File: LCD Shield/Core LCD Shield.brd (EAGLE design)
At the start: 115.6 x 54.6 mm, 7 parts

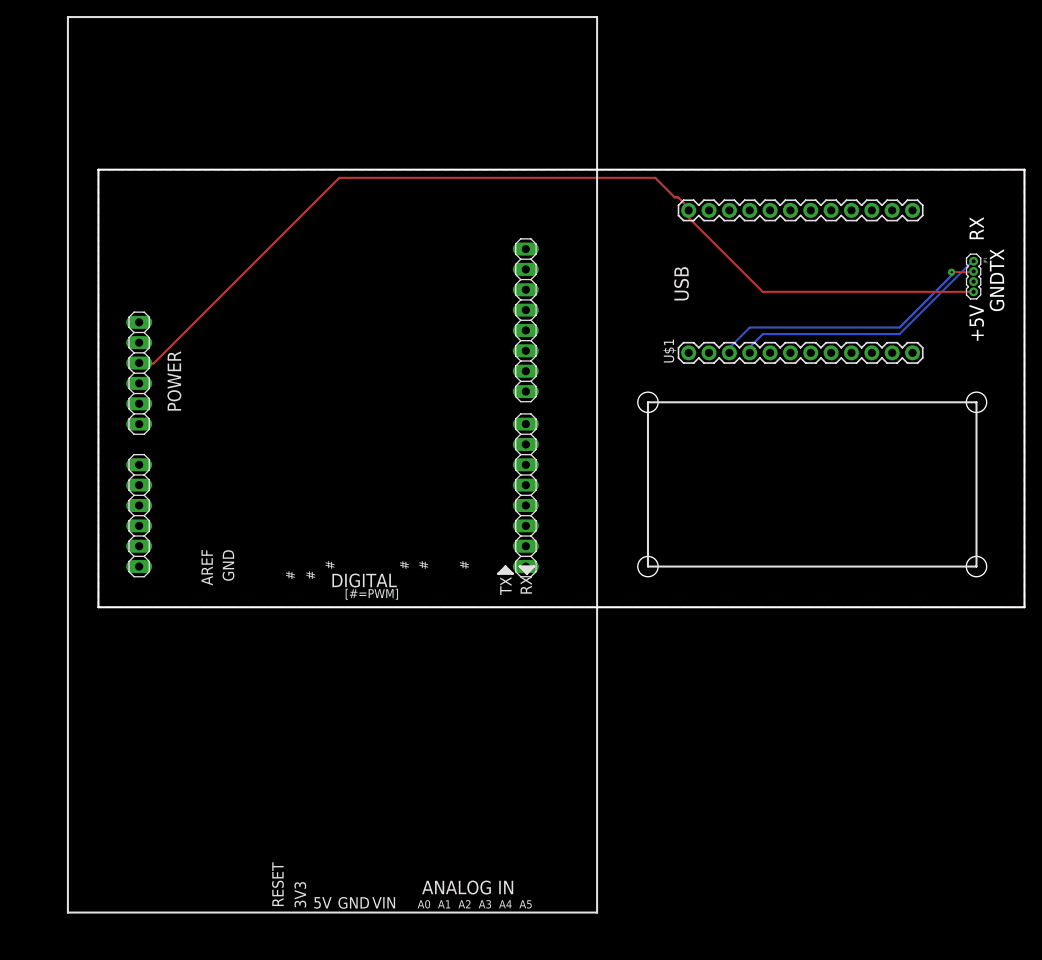
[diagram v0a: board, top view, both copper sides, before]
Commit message: WIP: Created infinity camera from Shield Shield template.
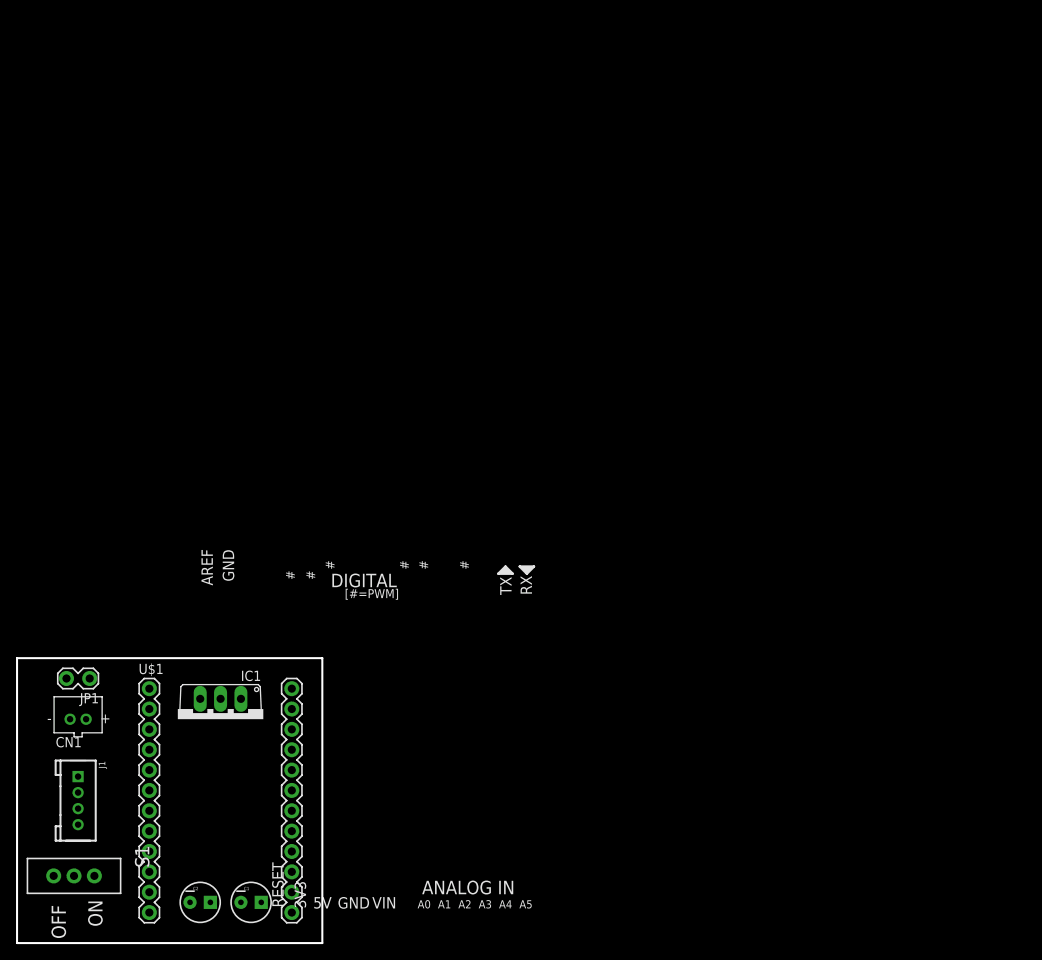
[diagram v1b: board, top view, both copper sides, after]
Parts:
- removed AD, POWER: (no value), pinhead:1X06
- removed IOH, IOL: (no value), pinhead:1X08
- removed U$2: (no value), Spark:SPARK_LOGO
- added C1: 10uF, SparkFun-Capacitors:CPOL-RADIAL-10UF-25V
- added C2: 1uF, SparkFun-Capacitors:CPOL-RADIAL-10UF-25V
- added CN1: (no value), adafruit:JST-PH-2-THM
- added IC1: MC33269T-5.0, linear:TO220V
- added J1: TWIG_2.0-DIP-FEMALE, Connector:2.0_1X4
- added S1: (no value), SparkFun-Electromechanical:SWITCH-SPDT
- JP1: device SparkFun-Connectors:1X04-1.27MM -> SparkFun-Connectors:1X02_LOCK
- moved JP1 122.1 mm to (8.89, 33.0), turned to 180 degrees
- moved U$1 97.1 mm to (25.4, 17.8), turned to 0 degrees
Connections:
- removed net RAW: U$1.1
- new net +3V3: U$1.24
- new net N1: C1.1, IC1.2, S1.2
- new net RESET: U$1.23
- new net VIN: C2.1, CN1.1, IC1.3, JP1.1, U$1.1
- net +5V: now also J1.3, S1.1; no longer JP1.4, POWER.3, U$1.24
- net GND: now also C1.2, C2.2, CN1.2, IC1.1, J1.4, JP1.2; no longer IOH.7, JP1.3, POWER.4, POWER.5
- net RX: now also J1.2; no longer JP1.1
- net TX: now also J1.1; no longer JP1.2
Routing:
- net +5V: track 120.9 -> 0.00 mm
- net TX: track 35.5 -> 0.00 mm, vias 1 -> 0
- net RX: track 33.1 -> 0.00 mm
- removed copper zone on layer 1, net GND
- removed copper zone on layer 16, net GND
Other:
- board size 115.6 x 54.6 mm -> 38.1 x 35.6 mm
- board text added: "OFF"
- board text added: "ON"
- board text removed: "+5V"
- board text removed: "USB"
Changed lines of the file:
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@@
 <rectangle x1="90.7098" y1="32.6327" x2="94.5833" y2="32.6454" layer="201"/>
 <rectangle x1="87.5348" y1="32.6327" x2="90.7098" y2="32.6454" layer="201"/>
-<wire x1="6.35" y1="3.81" x2="6.35" y2="115.57" width="0.254" layer="21"/>
-<wire x1="6.35" y1="115.57" x2="72.39" y2="115.57" width="0.254" layer="21"/>
-<wire x1="72.39" y1="115.57" x2="72.39" y2="3.81" width="0.254" layer="21"/>
-<wire x1="72.39" y1="3.81" x2="6.35" y2="3.81" width="0.254" layer="21"/>
-<hole x="119.74" y="46.99" drill="2.54"/>
-<hole x="78.74" y="46.99" drill="2.54"/>
-<hole x="78.74" y="67.49" drill="2.54"/>
-<hole x="119.74" y="67.49" drill="2.54"/>
-<wire x1="10.16" y1="41.91" x2="10.16" y2="96.52" width="0.254" layer="20"/>
-<wire x1="10.16" y1="96.52" x2="125.73" y2="96.52" width="0.254" layer="20"/>
-<wire x1="125.73" y1="96.52" x2="125.73" y2="41.91" width="0.254" layer="20"/>
-<wire x1="125.73" y1="41.91" x2="10.16" y2="41.91" width="0.254" layer="20"/>
-<text x="120.65" y="74.93" size="1.778" layer="20" font="vector" ratio="15" rot="R90">+5V</text>
-<text x="123.19" y="78.74" size="1.778" layer="20" font="vector" ratio="15" rot="R90">GND</text>
-<text x="123.19" y="83.82" size="1.778" layer="20" font="vector" ratio="15" rot="R90">TX</text>
-<text x="120.65" y="87.63" size="1.778" layer="20" font="vector" ratio="15" rot="R90">RX</text>
-<wire x1="78.74" y1="46.99" x2="78.74" y2="67.49" width="0.254" layer="21"/>
-<wire x1="78.74" y1="67.49" x2="119.74" y2="67.49" width="0.254" layer="21"/>
-<wire x1="119.74" y1="67.49" x2="119.74" y2="46.99" width="0.254" layer="21"/>
-<wire x1="119.74" y1="46.99" x2="78.74" y2="46.99" width="0.254" layer="21"/>
-<text x="83.82" y="80.01" size="1.778" layer="21" font="vector" ratio="15" rot="R90">USB</text>
+<text x="10.668" y="2.032" size="1.778" layer="21" ratio="15" rot="R90">ON</text>
+<text x="6.096" y="0.508" size="1.778" layer="21" ratio="15" rot="R90">OFF</text>
+<wire x1="0" y1="0" x2="0" y2="35.56" width="0.254" layer="20"/>
+<wire x1="0" y1="35.56" x2="38.1" y2="35.56" width="0.254" layer="20"/>
+<wire x1="38.1" y1="35.56" x2="38.1" y2="0" width="0.254" layer="20"/>
+<wire x1="38.1" y1="0" x2="0" y2="0" width="0.254" layer="20"/>
 </plain>
 <attributes>
@@
 </autorouter>
 <elements>
-<element name="IOL" library="pinhead" package="1X08" value="" x="63.5" y="55.88" smashed="yes" rot="R90">
-<attribute name="VALUE" x="66.675" y="45.72" size="1.27" layer="27" rot="R90"/>
-</element>
-<element name="IOH" library="pinhead" package="1X08" value="" x="63.5" y="77.724" smashed="yes" rot="R90">
-<attribute name="VALUE" x="66.675" y="67.564" size="1.27" layer="27" rot="R90"/>
-</element>
-<element name="AD" library="pinhead" package="1X06" value="" x="15.24" y="53.34" smashed="yes" rot="R270">
-<attribute name="VALUE" x="12.065" y="60.96" size="1.27" layer="27" rot="R270"/>
-</element>
-<element name="POWER" library="pinhead" package="1X06" value="" x="15.24" y="71.12" smashed="yes" rot="R270">
-<attribute name="NAME" x="18.796" y="73.914" size="1.6764" layer="25" font="vector" ratio="15" rot="R270"/>
-<attribute name="VALUE" x="12.065" y="78.74" size="1.27" layer="27" rot="R270"/>
-</element>
-<element name="U$1" library="Spark" package="SPARK_CORE" value="SPARK_CORECORE" x="97.79" y="82.55" rot="R90"/>
-<element name="U$2" library="Spark" package="SPARK_LOGO" value="" x="7.62" y="5.08"/>
-<element name="JP1" library="SparkFun-Connectors" package="1X04-1.27MM" value="" x="119.38" y="85.09" rot="R270"/>
+<element name="U$1" library="Spark" package="SPARK_CORE" value="SPARK_CORECORE" x="25.4" y="17.78"/>
+<element name="IC1" library="linear" package="TO220V" value="MC33269T-5.0" x="25.4" y="27.94" rot="R180"/>
+<element name="C1" library="SparkFun-Capacitors" package="CPOL-RADIAL-10UF-25V" value="10uF" x="29.21" y="5.08"/>
+<element name="C2" library="SparkFun-Capacitors" package="CPOL-RADIAL-10UF-25V" value="1uF" x="22.86" y="5.08"/>
+<element name="CN1" library="adafruit" package="JST-PH-2-THM" value="" x="7.62" y="27.94"/>
+<element name="JP1" library="SparkFun-Connectors" package="1X02_LOCK" value="" x="8.89" y="33.02" rot="R180"/>
+<element name="S1" library="SparkFun-Electromechanical" package="SWITCH-SPDT" value="" x="7.112" y="8.382" rot="R270"/>
+<element name="J1" library="Connector" package="2.0_1X4" value="TWIG_2.0-DIP-FEMALE" x="7.62" y="17.78" rot="R270"/>
 </elements>
 <signals>
 <signal name="+5V">
-<contactref element="POWER" pad="3"/>
-<contactref element="U$1" pad="24"/>
-<contactref element="JP1" pad="4"/>
-<wire x1="93.0656" y1="81.28" x2="119.38" y2="81.28" width="0.254" layer="1"/>
-<wire x1="83.7184" y1="90.6272" x2="93.0656" y2="81.28" width="0.254" layer="1"/>
-<wire x1="83.7184" y1="91.44" x2="83.7184" y2="90.6272" width="0.254" layer="1"/>
-<wire x1="83.7184" y1="91.44" x2="83.82" y2="91.44" width="0.254" layer="1"/>
-<wire x1="17.0688" y1="72.3392" x2="15.4432" y2="72.3392" width="0.254" layer="1"/>
-<wire x1="40.2336" y1="95.504" x2="17.0688" y2="72.3392" width="0.254" layer="1"/>
-<wire x1="79.6544" y1="95.504" x2="40.2336" y2="95.504" width="0.254" layer="1"/>
-<wire x1="82.0928" y1="93.0656" x2="79.6544" y2="95.504" width="0.254" layer="1"/>
-<wire x1="82.4992" y1="93.0656" x2="82.0928" y2="93.0656" width="0.254" layer="1"/>
-<wire x1="84.1248" y1="91.44" x2="82.4992" y2="93.0656" width="0.254" layer="1"/>
-<wire x1="15.4432" y1="72.3392" x2="15.24" y2="72.39" width="0.254" layer="1"/>
-<wire x1="84.1248" y1="91.44" x2="83.82" y2="91.44" width="0.254" layer="1"/>
+<contactref element="S1" pad="1"/>
+<contactref element="J1" pad="3"/>
+<wire x1="9.652" y1="8.382" x2="7.62" y2="16.78" width="0" layer="19" extent="1-1"/>
 </signal>
 <signal name="GND">
-<contactref element="IOH" pad="7"/>
-<contactref element="POWER" pad="5"/>
-<contactref element="POWER" pad="4"/>
 <contactref element="U$1" pad="2"/>
 <contactref element="U$1" pad="21"/>
-<contactref element="JP1" pad="3"/>
-<polygon width="0.254" layer="1">
-<vertex x="10.16" y="41.91"/>
-<vertex x="10.16" y="96.52"/>
-<vertex x="125.73" y="96.52"/>
-<vertex x="125.73" y="41.91"/>
-</polygon>
-<polygon width="0.254" layer="16">
-<vertex x="10.16" y="41.91"/>
-<vertex x="10.16" y="96.52"/>
-<vertex x="125.73" y="96.52"/>
-<vertex x="125.73" y="41.91"/>
-</polygon>
+<contactref element="IC1" pad="1"/>
+<contactref element="C2" pad="2"/>
+<contactref element="C1" pad="2"/>
+<contactref element="CN1" pad="2"/>
+<contactref element="JP1" pad="2"/>
+<contactref element="J1" pad="4"/>
+<wire x1="34.29" y1="24.13" x2="27.94" y2="30.48" width="0" layer="19" extent="1-1"/>
+<wire x1="16.51" y1="29.21" x2="27.94" y2="30.48" width="0" layer="19" extent="1-1"/>
+<wire x1="6.62" y1="27.94" x2="16.51" y2="29.21" width="0" layer="19" extent="1-1"/>
+<wire x1="6.1722" y1="33.02" x2="6.62" y2="27.94" width="0" layer="19" extent="1-1"/>
+<wire x1="7.62" y1="14.78" x2="6.62" y2="27.94" width="0" layer="19" extent="1-1"/>
+<wire x1="21.59" y1="5.08" x2="7.62" y2="14.78" width="0" layer="19" extent="1-1"/>
+<wire x1="27.94" y1="5.08" x2="21.59" y2="5.08" width="0" layer="19" extent="1-1"/>
+</signal>
+<signal name="RESET">
+<contactref element="U$1" pad="23"/>
+</signal>
+<signal name="VIN">
+<contactref element="U$1" pad="1"/>
+<contactref element="IC1" pad="3"/>
+<contactref element="C2" pad="1"/>
+<contactref element="CN1" pad="1"/>
+<contactref element="JP1" pad="1"/>
+<wire x1="16.51" y1="31.75" x2="22.86" y2="30.48" width="0" layer="19" extent="1-1"/>
+<wire x1="9.0678" y1="33.02" x2="16.51" y2="31.75" width="0" layer="19" extent="1-1"/>
+<wire x1="8.62" y1="27.94" x2="9.0678" y2="33.02" width="0" layer="19" extent="1-1"/>
+<wire x1="24.13" y1="5.08" x2="22.86" y2="30.48" width="0" layer="19" extent="1-1"/>
+</signal>
+<signal name="+3V3">
+<contactref element="U$1" pad="24"/>
+</signal>
+<signal name="N1">
+<contactref element="IC1" pad="2"/>
+<contactref element="C1" pad="1"/>
+<contactref element="S1" pad="2"/>
+<wire x1="30.48" y1="5.08" x2="25.4" y2="30.48" width="0" layer="19" extent="1-1"/>
+<wire x1="7.112" y1="8.382" x2="30.48" y2="5.08" width="0" layer="19" extent="1-1"/>
 </signal>
 <signal name="VDDA">
 <contactref element="U$1" pad="22"/>
 </signal>
-<signal name="RAW">
-<contactref element="U$1" pad="1"/>
+<signal name="RX">
+<contactref element="J1" pad="2"/>
+<contactref element="U$1" pad="4"/>
+<wire x1="7.62" y1="18.78" x2="16.51" y2="24.13" width="0" layer="19" extent="1-1"/>
 </signal>
 <signal name="TX">
-<contactref element="JP1" pad="2"/>
+<contactref element="J1" pad="1"/>
 <contactref element="U$1" pad="3"/>
-<wire x1="116.6368" y1="83.7184" x2="119.0752" y2="83.7184" width="0.254" layer="1"/>
-<wire x1="116.6368" y1="83.312" x2="116.6368" y2="83.7184" width="0.254" layer="16"/>
-<wire x1="110.1344" y1="76.8096" x2="116.6368" y2="83.312" width="0.254" layer="16"/>
-<wire x1="91.44" y1="76.8096" x2="110.1344" y2="76.8096" width="0.254" layer="16"/>
-<wire x1="88.5952" y1="73.9648" x2="91.44" y2="76.8096" width="0.254" layer="16"/>
-<wire x1="119.0752" y1="83.7184" x2="119.38" y2="83.82" width="0.254" layer="1"/>
-<wire x1="88.5952" y1="73.9648" x2="88.9" y2="73.66" width="0.254" layer="16"/>
-<via x="116.6368" y="83.7184" extent="1-16" drill="0.3048"/>
-</signal>
-<signal name="RX">
-<contactref element="JP1" pad="1"/>
-<contactref element="U$1" pad="4"/>
-<wire x1="110.1344" y1="75.9968" x2="119.0752" y2="84.9376" width="0.254" layer="16"/>
-<wire x1="93.0656" y1="75.9968" x2="110.1344" y2="75.9968" width="0.254" layer="16"/>
-<wire x1="91.44" y1="74.3712" x2="93.0656" y2="75.9968" width="0.254" layer="16"/>
-<wire x1="91.44" y1="73.66" x2="91.44" y2="74.3712" width="0.254" layer="16"/>
-<wire x1="119.0752" y1="84.9376" x2="119.38" y2="85.09" width="0.254" layer="16"/>
+<wire x1="7.62" y1="20.78" x2="16.51" y2="26.67" width="0" layer="19" extent="1-1"/>
 </signal>
 </signals>
